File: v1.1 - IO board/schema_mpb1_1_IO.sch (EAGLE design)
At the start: 94 parts

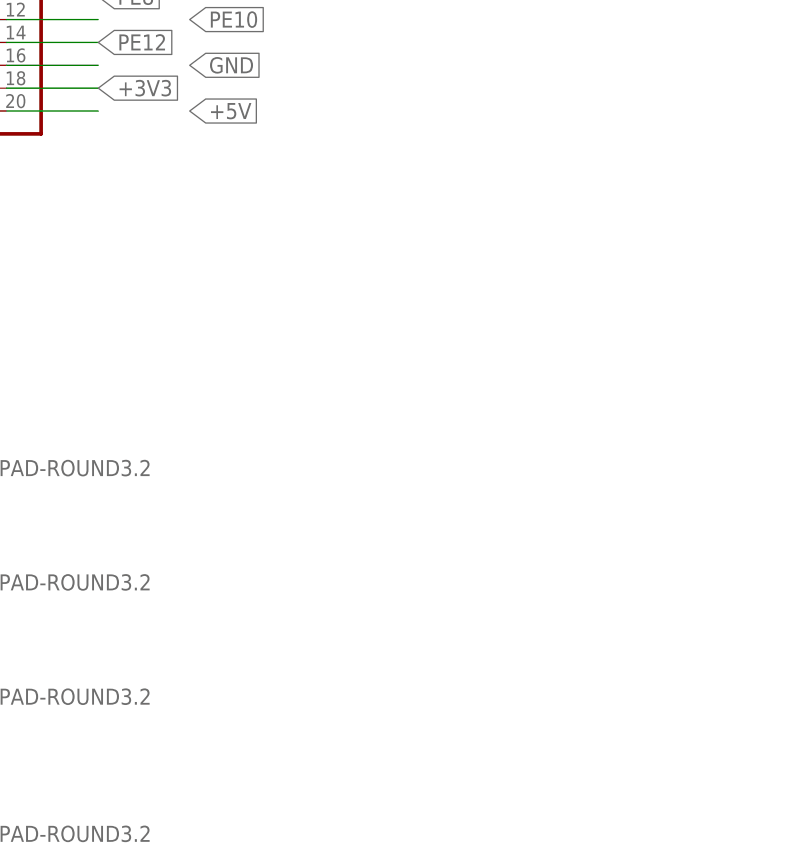
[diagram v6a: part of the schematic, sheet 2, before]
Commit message: IO board revision
- Made Output traces thicker
- Added pad for 5V/3.3V power for input sensors
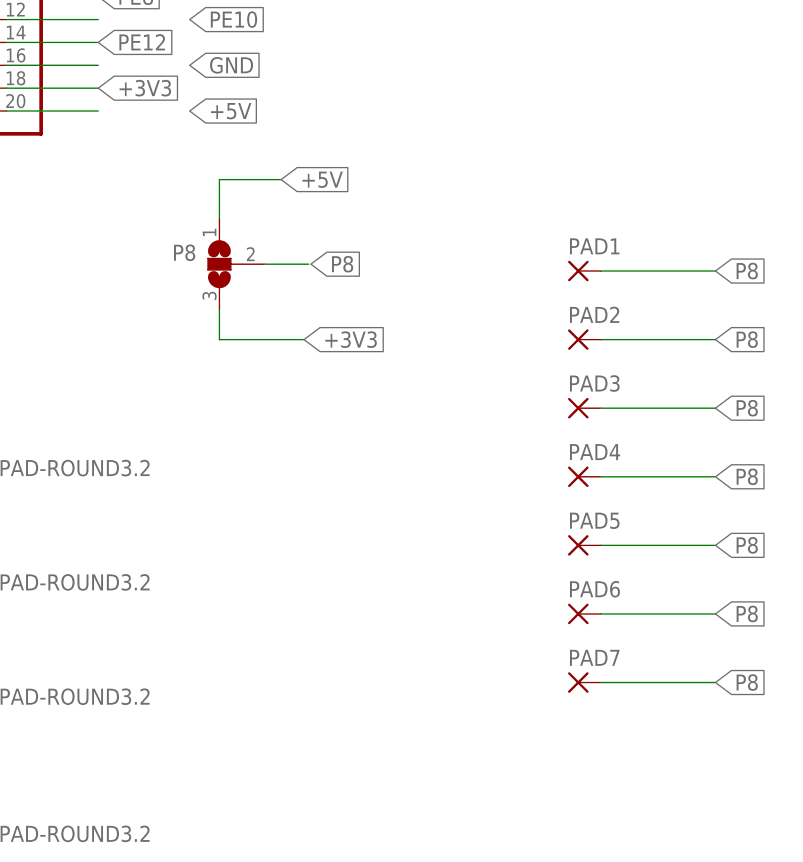
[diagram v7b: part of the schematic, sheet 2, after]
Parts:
- added P8: (no value), jumper:SJ2WW
- added PAD1, PAD2, PAD3, PAD4, PAD5, PAD6, PAD7: (no value), wirepad:SMD2
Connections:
- new net P8: P8.2, PAD1.P, PAD2.P, PAD3.P, PAD4.P, PAD5.P, PAD6.P, PAD7.P
- net +3V3: now also P8.3
- net +5V: now also P8.1
